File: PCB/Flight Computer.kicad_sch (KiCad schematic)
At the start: 0 parts

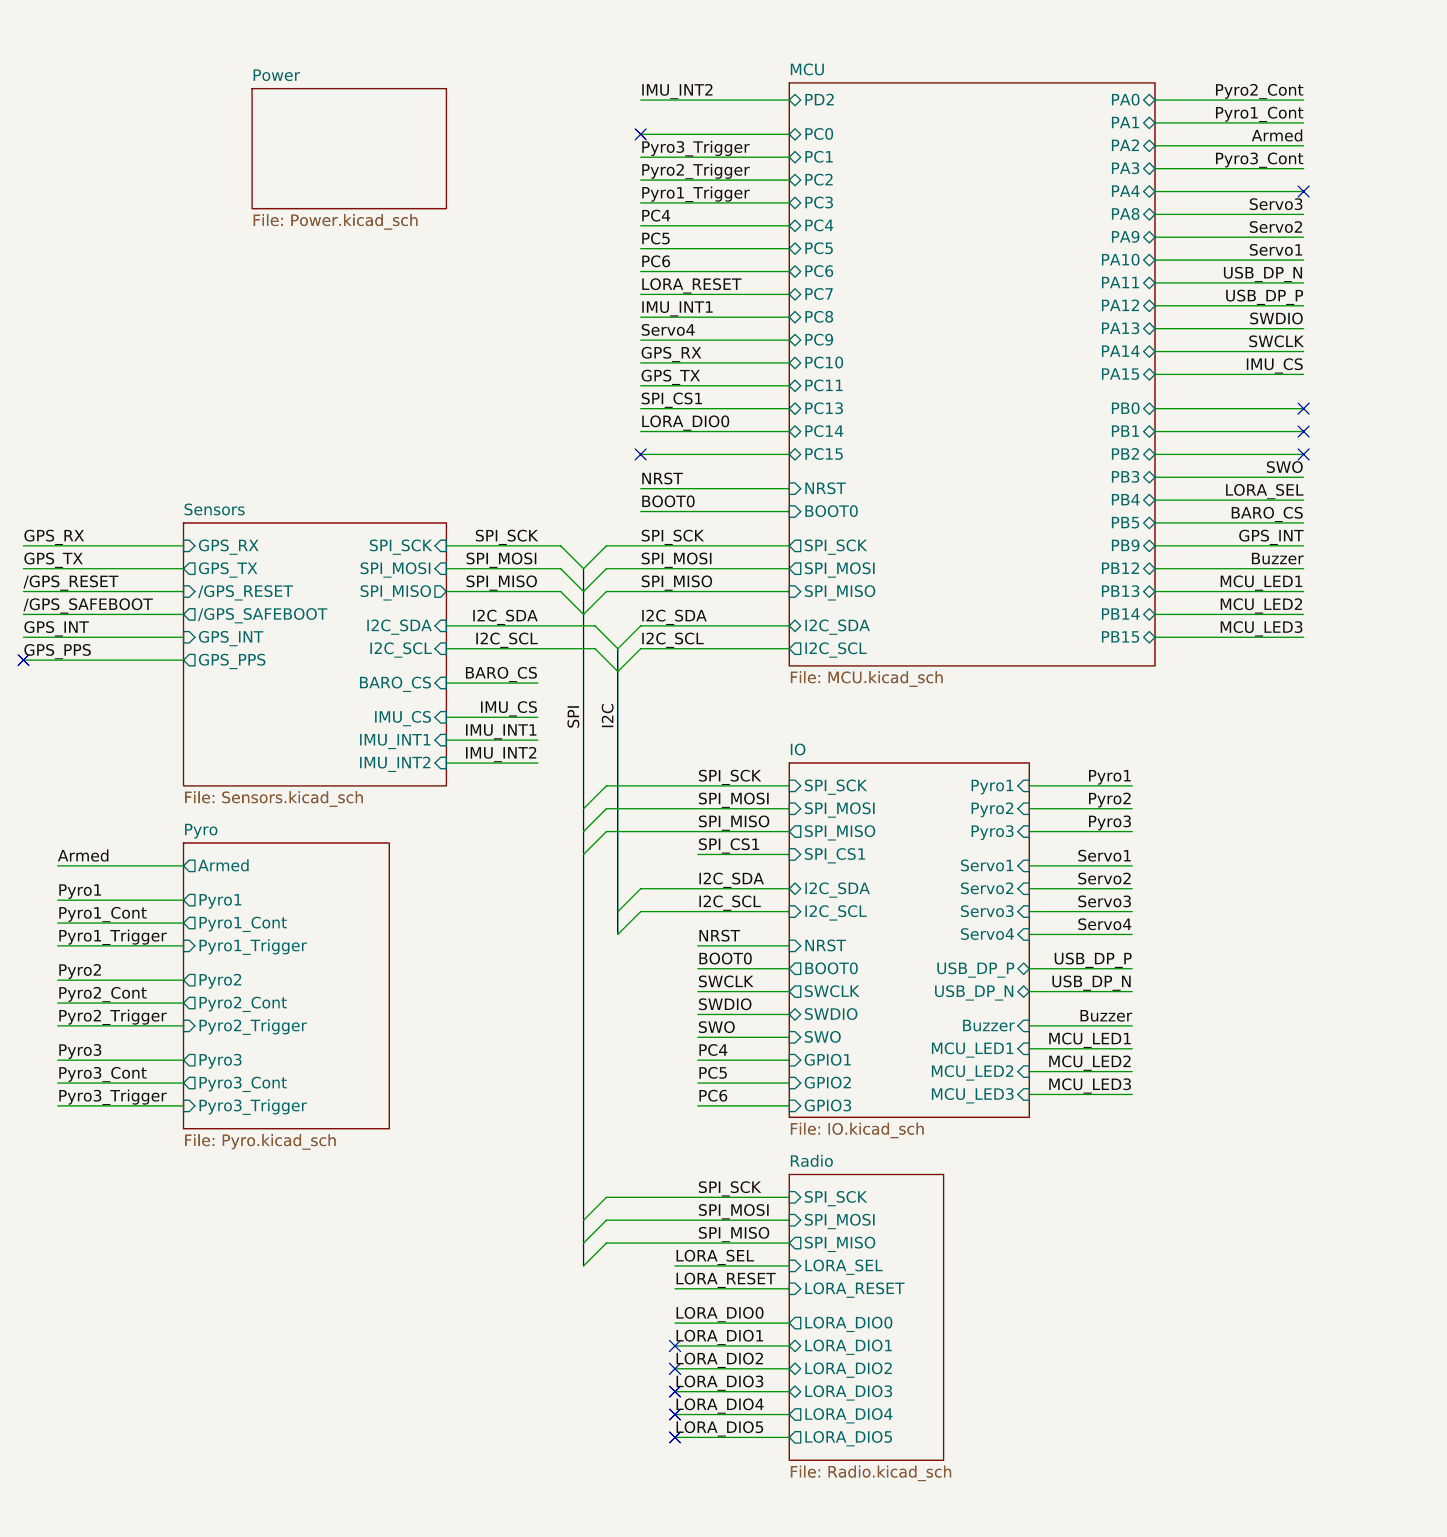
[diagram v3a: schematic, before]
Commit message: - Swapped out 2 LED's for neopixels- Added reverse polarity protection- Replaced Radio module with deticated IC and passives
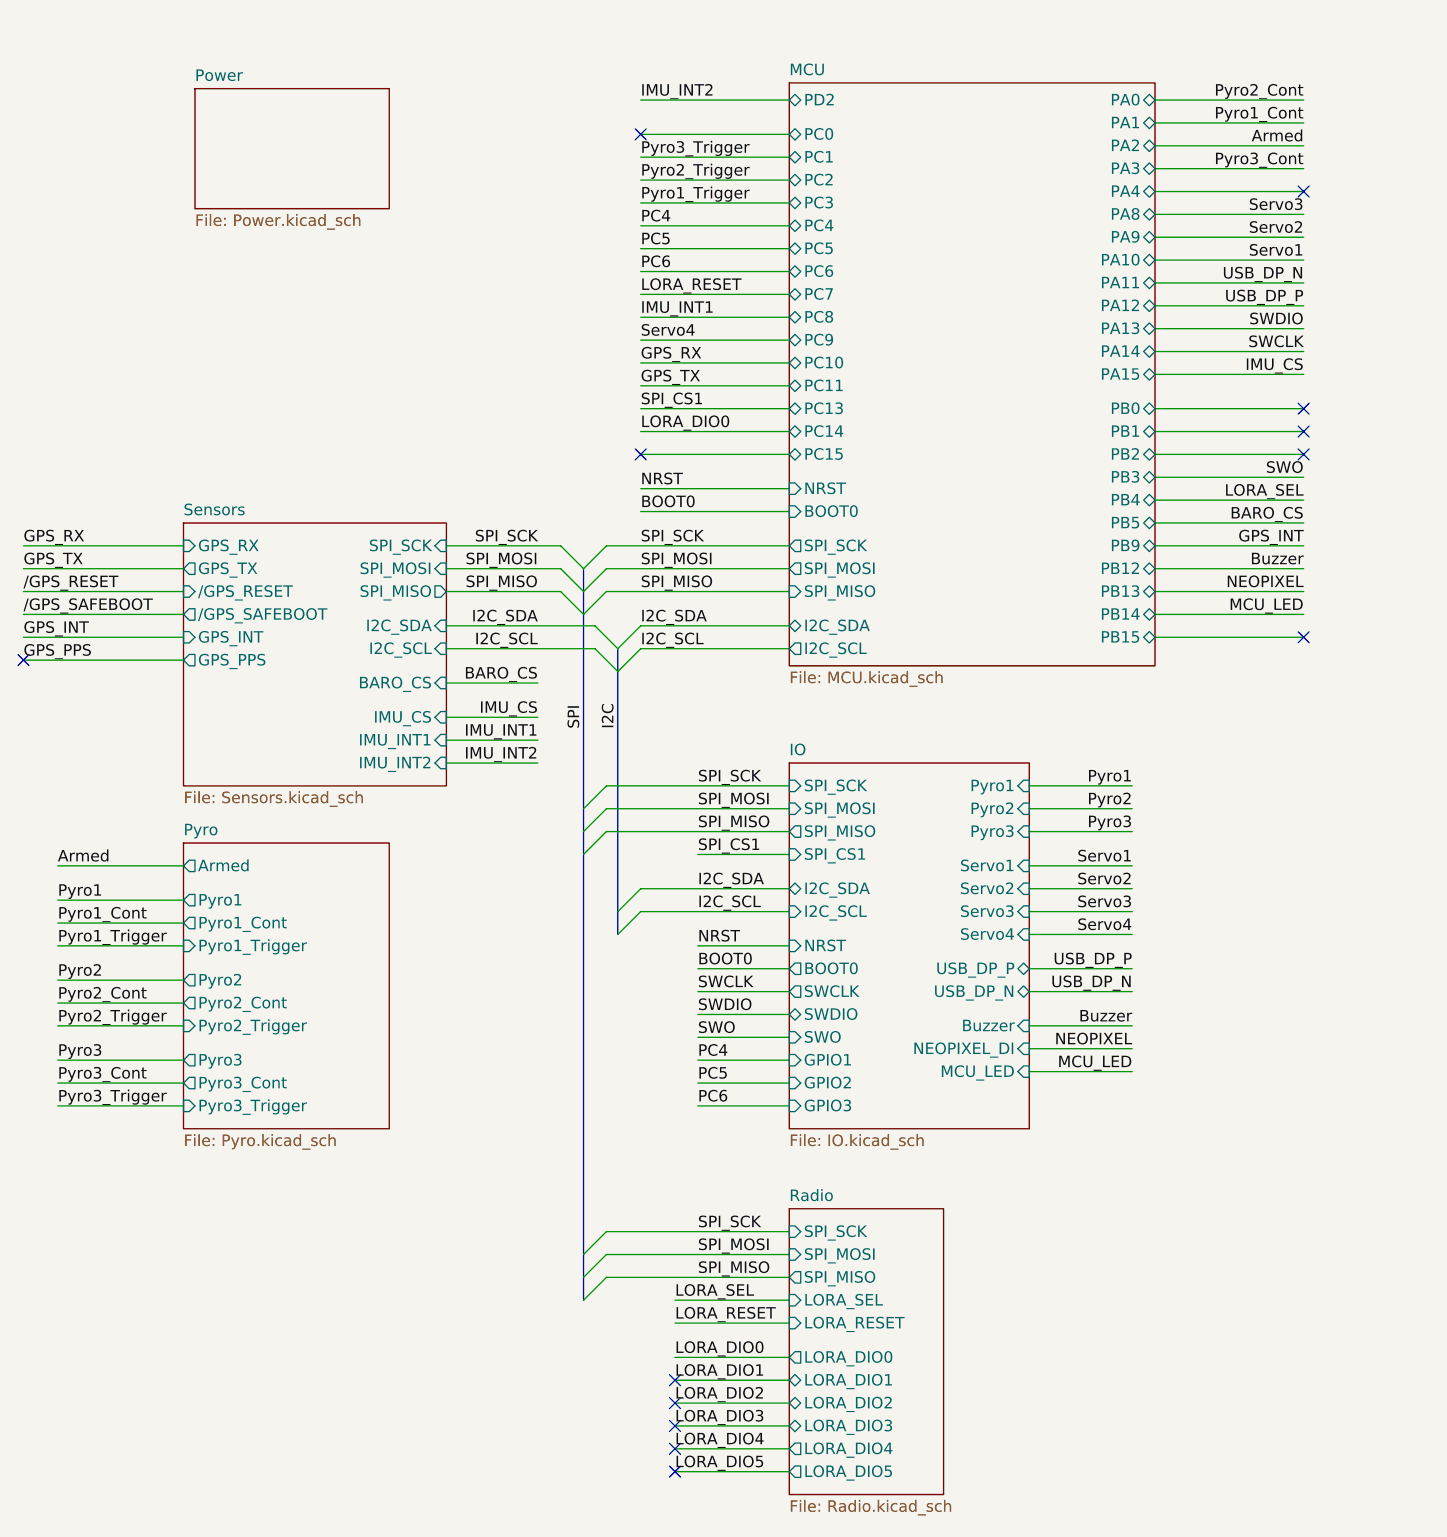
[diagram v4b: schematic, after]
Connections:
- no-connect marks 12 -> 13
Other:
- sheet IO ports: added MCU_LED, NEOPIXEL_DI; removed MCU_LED1, MCU_LED2, MCU_LED3

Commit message: Routed PCB
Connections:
- no-connect marks 13 -> 15
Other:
- sheet MCU ports: added PB7, PB8; removed none

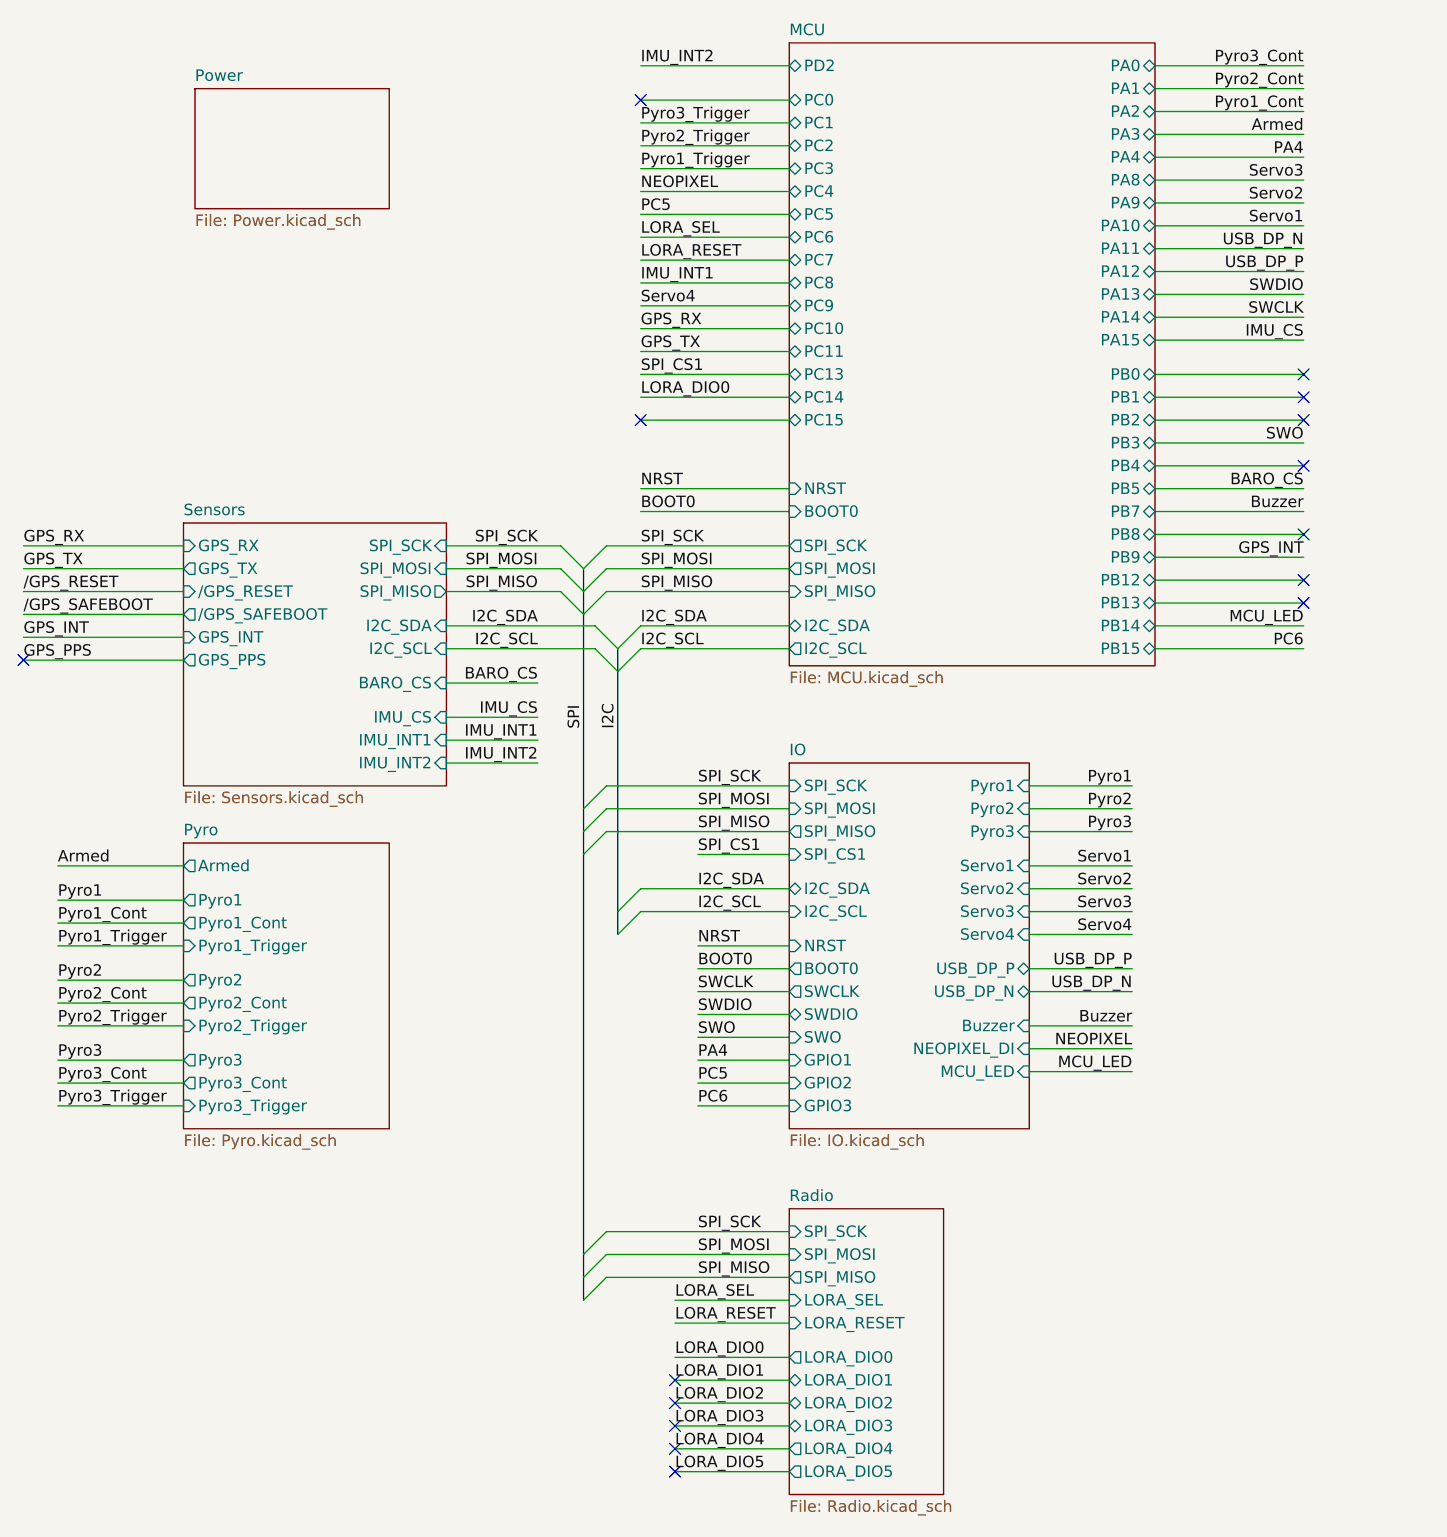
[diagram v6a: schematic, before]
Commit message: Changed pin mappings a tad. Added courtyards to some parts that were missing them
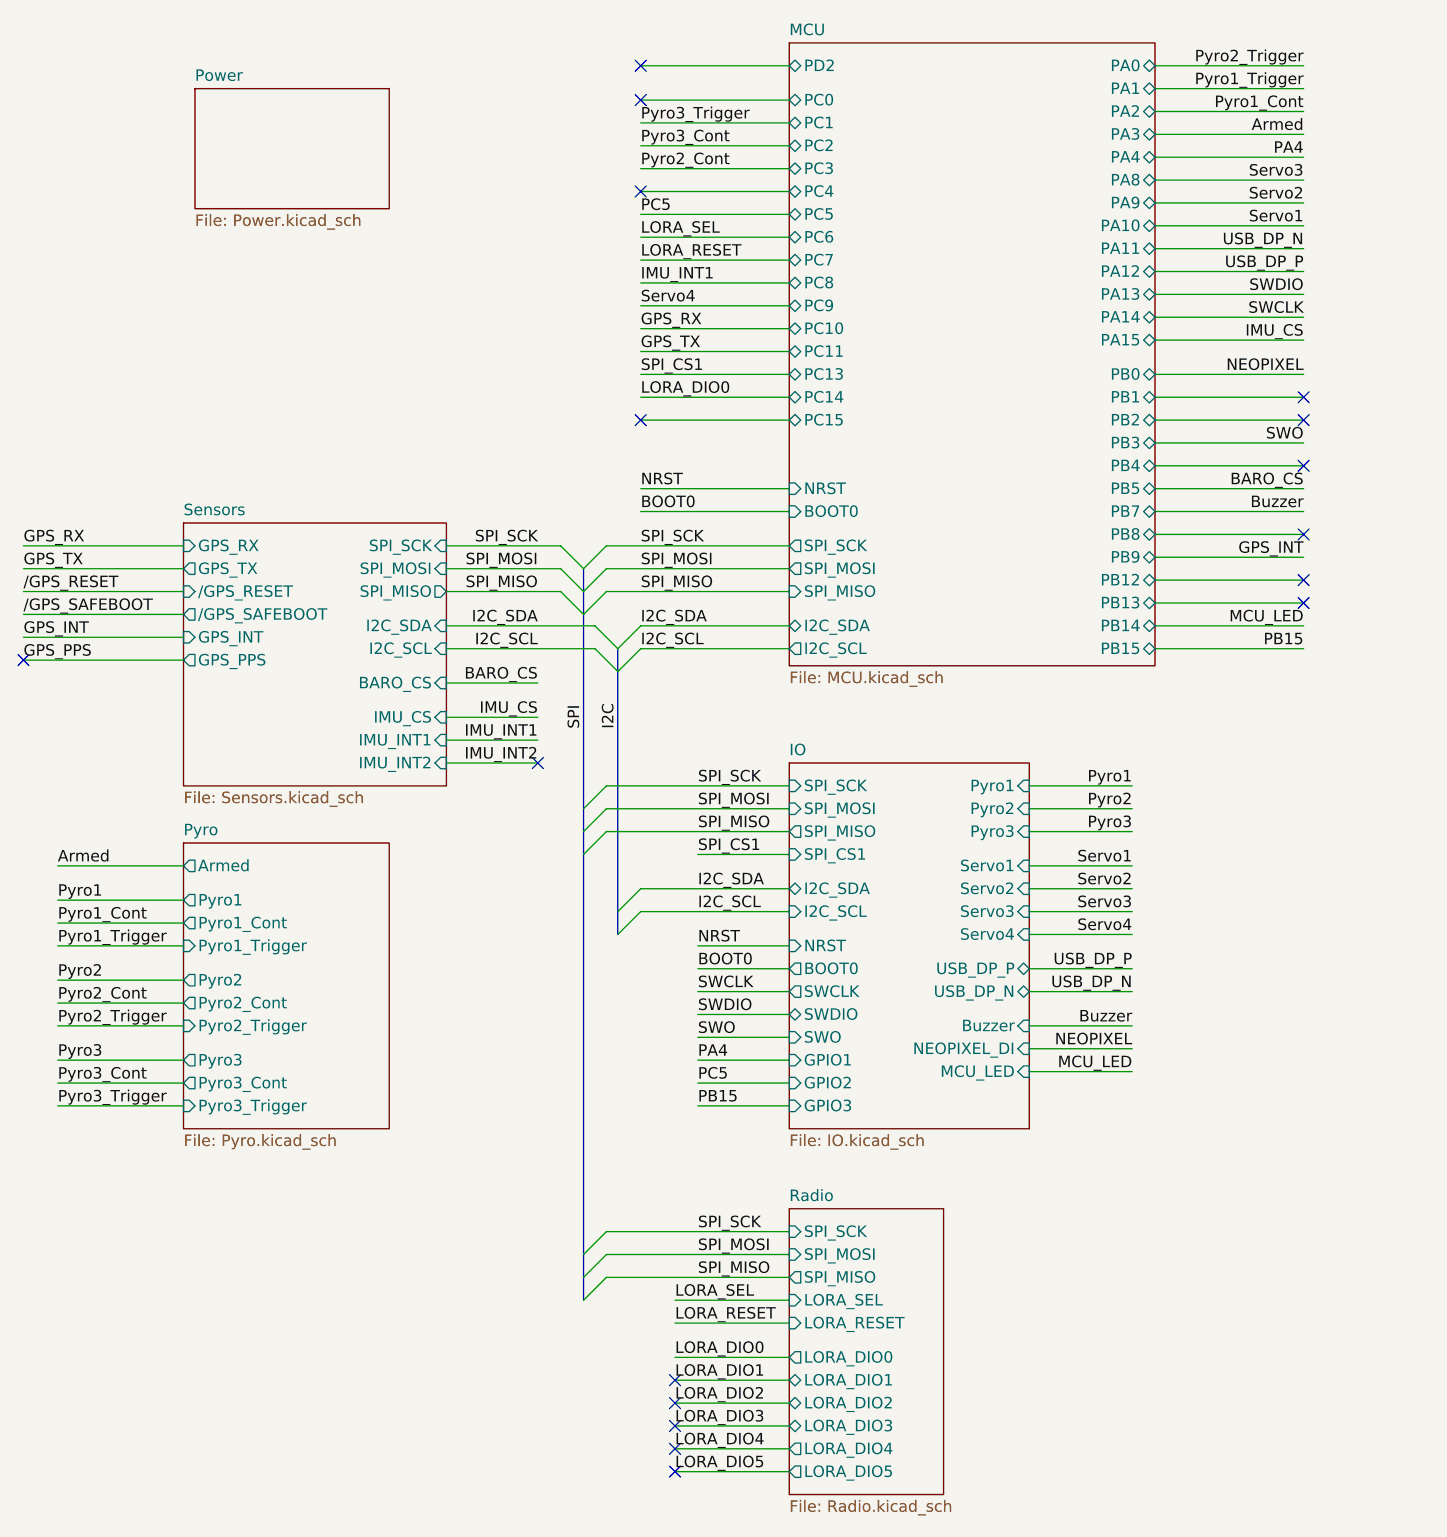
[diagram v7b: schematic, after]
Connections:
- no-connect marks 15 -> 17
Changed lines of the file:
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@@
-	)
-	(no_connect
-		(at 173.99 62.23)
 	)
 	(no_connect
@@
 	)
 	(no_connect
+		(at 100.33 41.91)
+	)
+	(no_connect
 		(at 173.99 72.39)
 	)
@@
 	)
 	(no_connect
+		(at 88.9 105.41)
+	)
+	(no_connect
 		(at 173.99 85.09)
+	)
+	(no_connect
+		(at 100.33 27.94)
 	)
 	(no_connect
@@
 		)
 	)
-	(label "Pyro1_Trigger"
-		(at 100.33 39.37 0)
-		(effects
-			(font
-				(size 1.27 1.27)
-			)
-			(justify left bottom)
-		)
-	)
 	(label "Pyro3_Trigger"
 		(at 100.33 34.29 0)
@@
 		)
 	)
-	(label "PC6"
+	(label "PB15"
 		(at 106.68 143.51 0)
 		(effects
@@
 		)
 	)
+	(label "Pyro1_Trigger"
+		(at 173.99 30.48 180)
+		(effects
+			(font
+				(size 1.27 1.27)
+			)
+			(justify right bottom)
+		)
+	)
+	(label "NEOPIXEL"
+		(at 173.99 62.23 180)
+		(effects
+			(font
+				(size 1.27 1.27)
+			)
+			(justify right bottom)
+		)
+	)
 	(label "SPI_SCK"
 		(at 88.9 81.28 180)
@@
 		)
 	)
-	(label "Pyro3_Cont"
-		(at 173.99 27.94 180)
-		(effects
-			(font
-				(size 1.27 1.27)
-			)
-			(justify right bottom)
-		)
-	)
 	(label "GPS_INT"
 		(at 173.99 82.55 180)
@@
 		)
 	)
+	(label "Pyro2_Trigger"
+		(at 173.99 27.94 180)
+		(effects
+			(font
+				(size 1.27 1.27)
+			)
+			(justify right bottom)
+		)
+	)
 	(label "USB_DP_N"
 		(at 154.94 130.81 180)
@@
 		)
 	)
-	(label "PC6"
+	(label "PB15"
 		(at 173.99 92.71 180)
 		(effects
@@
 		)
 	)
-	(label "IMU_INT2"
-		(at 100.33 27.94 0)
-		(effects
-			(font
-				(size 1.27 1.27)
-			)
-			(justify left bottom)
-		)
-	)
-	(label "Pyro2_Trigger"
-		(at 100.33 36.83 0)
-		(effects
-			(font
-				(size 1.27 1.27)
-			)
-			(justify left bottom)
-		)
-	)
-	(label "Pyro2_Cont"
-		(at 173.99 30.48 180)
-		(effects
-			(font
-				(size 1.27 1.27)
-			)
-			(justify right bottom)
-		)
-	)
 	(label "BARO_CS"
 		(at 173.99 74.93 180)
@@
 		)
 	)
+	(label "Pyro3_Cont"
+		(at 100.33 36.83 0)
+		(effects
+			(font
+				(size 1.27 1.27)
+			)
+			(justify left bottom)
+		)
+	)
 	(label "LORA_DIO5"
 		(at 104.14 184.15 0)
@@
 		)
 	)
+	(label "Pyro2_Cont"
+		(at 100.33 39.37 0)
+		(effects
+			(font
+				(size 1.27 1.27)
+			)
+			(justify left bottom)
+		)
+	)
 	(label "SPI_MOSI"
 		(at 88.9 83.82 180)
@@
 		)
 	)
-	(label "NEOPIXEL"
-		(at 100.33 41.91 0)
-		(effects
-			(font
-				(size 1.27 1.27)
-			)
-			(justify left bottom)
-		)
-	)
